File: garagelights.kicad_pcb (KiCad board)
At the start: 4 copper layers, 63.5 x 63.5 mm, 32 parts, among them J1 Conn_01x04, J2 Conn_01x06, Q1 ZVN4206AV, Q2 ZVN4206AV, Q3 ZVN4206AV, U1 NE555P, U2 NE555P, U3 4013, U4 LM7805_TO220, U5 4013

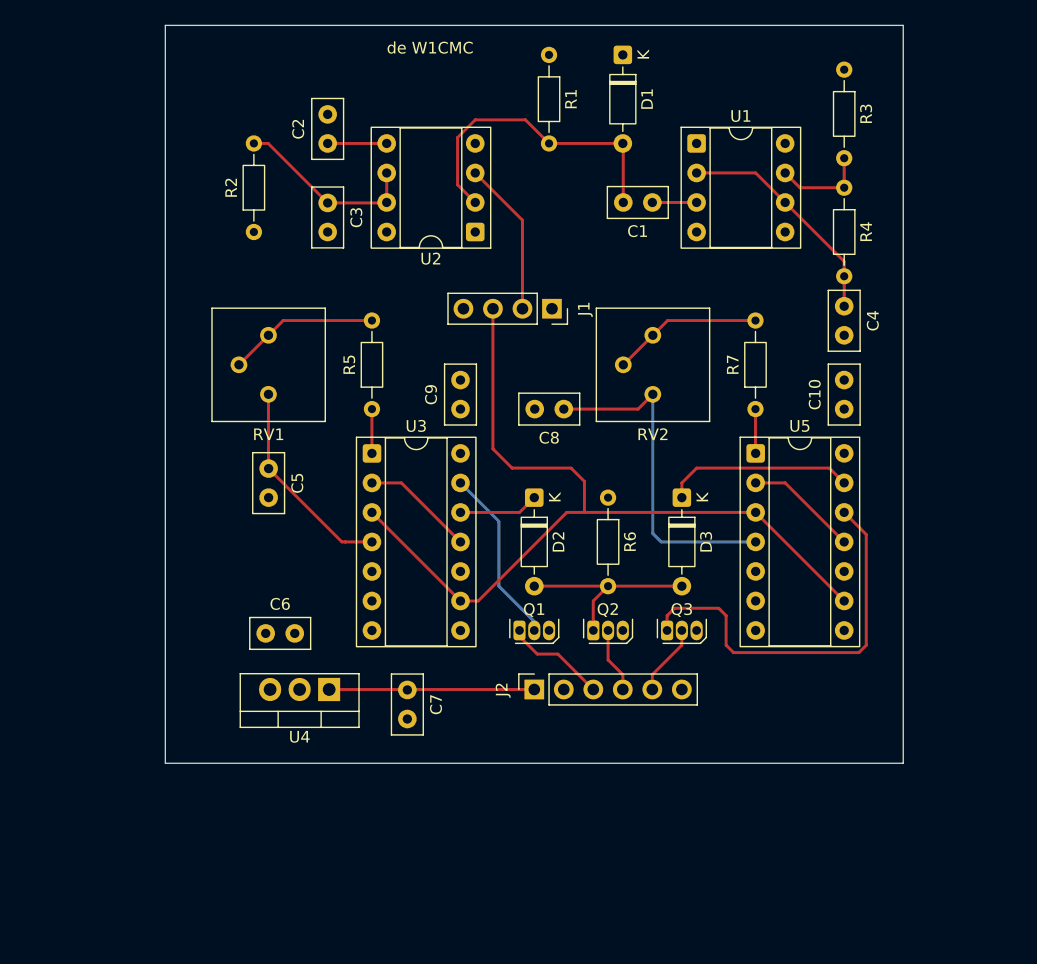
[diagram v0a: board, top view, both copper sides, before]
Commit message: Added screw terminals and mounting holes
Also working towards reducing the number of layers to two.
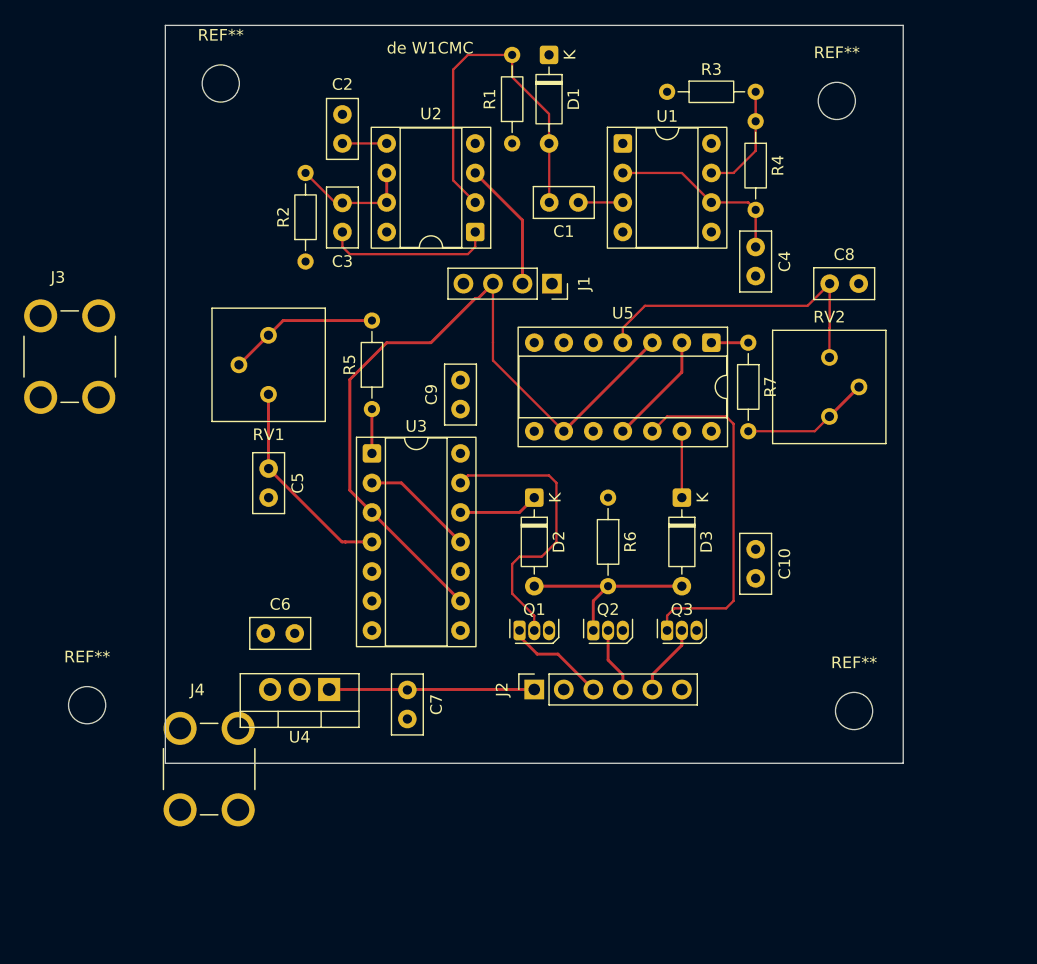
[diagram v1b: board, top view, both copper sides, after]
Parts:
- added J3: Screw_Terminal_01x01, Library:KEYSTONE_8191, F.Cu at (117.5, 92.0)
- added J4: Screw_Terminal_01x01, Library:KEYSTONE_8191, F.Cu at (129.5, 127.5)
- added REF**: MountingHole_3.2mm_M3, MountingHole:MountingHole_3.2mm_M3, F.Cu at (183.5, 70.0)
- added REF**: MountingHole_3.2mm_M3, MountingHole:MountingHole_3.2mm_M3, F.Cu at (185.0, 122.5)
- added REF**: MountingHole_3.2mm_M3, MountingHole:MountingHole_3.2mm_M3, F.Cu at (119.0, 122.0)
- added REF**: MountingHole_3.2mm_M3, MountingHole:MountingHole_3.2mm_M3, F.Cu at (130.5, 68.5)
- C5: value 0.1 -> 1 uF
- moved C8 25.3 mm to (182.9, 85.7), turned to 0 degrees
- moved RV2 16.7 mm to (182.9, 97.2), turned to 0 degrees
- moved R3 15.4 mm to (168.9, 69.2), turned to 0 degrees
- moved C10 14.3 mm to (176.5, 108.6), turned to -90 degrees
- moved U5 10.3 mm to (172.7, 90.8), turned to -90 degrees
- moved R4 9.53 mm to (176.5, 71.8)
- moved C4 9.17 mm to (176.5, 82.6)
- moved R1 8.25 mm to (155.6, 73.7), turned to 90 degrees
- moved C1 6.37 mm to (161.3, 78.7)
- moved D1 6.35 mm to (158.8, 66.0)
- moved U1 6.35 mm to (165.1, 73.7)
- moved R7 5.75 mm to (175.9, 90.8), turned to -90 degrees
- moved R2 5.12 mm to (137.8, 83.8)
- moved J1 2.16 mm to (159.0, 85.7)
- moved C2 1.27 mm to (141.0, 73.7)
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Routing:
- net GND: track 0.00 -> 14.5 mm
- net Net-(D3-K): track 16.3 -> 5.72 mm
- net Net-(Q1-G): track 15.3 -> 25.0 mm
- net Net-(J1-Pin_3): track 73.9 -> 64.7 mm
- net Net-(U2-DIS): track 16.1 -> 10.9 mm
- net Net-(D1-A): track 27.0 -> 31.8 mm
- net Net-(U1-THR): track 19.7 -> 15.9 mm
- net Net-(Q3-G): track 34.2 -> 30.5 mm
- net Net-(U5A-R): track 29.3 -> 27.0 mm
- net Net-(J1-Pin_2): track 13.4 -> 11.2 mm
- net Net-(R7-Pad2): track 13.0 -> 11.1 mm
- net Net-(U1-DIS): track 8.15 -> 9.68 mm
- net Net-(U2-CV): track 5.08 -> 3.81 mm
- net Net-(U5A-Q): track 3.84 -> 3.22 mm

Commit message: Kinda sorta Rev_A
Finished the layout and brought it down to two layers, one of which
is a ground plane. Imported missing 3D models.
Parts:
- removed the REF** at (183.5, 70.0)
- removed the REF** at (185.0, 122.5)
- removed the REF** at (119.0, 122.0)
- removed the REF** at (130.5, 68.5)
- added C11: 0.1, Capacitor_THT:C_Disc_D5.0mm_W2.5mm_P2.50mm, F.Cu at (158.8, 73.0)
- added C12: 0.1, Capacitor_THT:C_Disc_D5.0mm_W2.5mm_P2.50mm, F.Cu at (175.9, 73.3)
- added REF**: MountingHole_3.2mm_M3, MountingHole:MountingHole_3.2mm_M3, F.Cu at (135.3, 135.9)
- added REF**: MountingHole_3.2mm_M3, MountingHole:MountingHole_3.2mm_M3, F.Cu at (192.4, 72.4)
- added REF**: MountingHole_3.2mm_M3, MountingHole:MountingHole_3.2mm_M3, F.Cu at (135.3, 72.4)
- added REF**: MountingHole_3.2mm_M3, MountingHole:MountingHole_3.2mm_M3, F.Cu at (192.4, 135.9)
- moved J3 51.8 mm to (151.1, 131.4)
- moved J4 47.2 mm to (176.5, 131.4)
- moved R7 21.3 mm to (182.2, 111.1), turned to 0 degrees
- moved U5 19.6 mm to (182.2, 108.0), turned to 180 degrees
- moved C8 14.8 mm to (185.4, 100.3), turned to -90 degrees
- moved RV2 12.6 mm to (192.4, 105.4)
- moved D1 12.0 mm to (165.1, 76.2), turned to 90 degrees
- moved RV1 10.8 mm to (135.3, 101.0)
- moved C5 8.81 mm to (142.2, 106.1)
- moved R2 8.64 mm to (144.8, 88.9)
- moved C2 7.43 mm to (148.0, 76.2)
- moved C3 7.43 mm to (148.0, 81.3)
- moved R1 6.84 mm to (161.9, 76.2)
- moved U2 6.84 mm to (158.8, 83.8)
- moved J1 5.45 mm to (163.8, 88.3)
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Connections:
- Q2 pad 1: Net-(D2-A) -> Net-(J2-Pin_4)
- Q2 pad 2: Net-(J2-Pin_4) -> Net-(D2-A)
- Q3 pad 1: Net-(Q3-G) -> Net-(J2-Pin_5)
- Q3 pad 2: Net-(J2-Pin_5) -> Net-(Q3-G)
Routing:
- net Net-(J1-Pin_3): track 64.7 -> 91.3 mm
- net +12V: track 17.7 -> 0.00 mm
- net Net-(U5A-R): track 27.0 -> 10.2 mm
- net GND: track 14.5 -> 0.00 mm
- net Net-(Q3-G): track 30.5 -> 22.1 mm
- net Net-(U3A-R): track 17.9 -> 10.2 mm
- net Net-(J2-Pin_4): track 5.61 -> 9.75 mm
- net Net-(Q1-G): track 25.0 -> 21.8 mm
- net Net-(J2-Pin_3): track 8.75 -> 11.9 mm
- net Net-(D2-A): track 17.0 -> 14.0 mm
- net Net-(R5-Pad2): track 13.0 -> 10.4 mm
- net Net-(U2-DIS): track 10.9 -> 9.29 mm
- net Net-(U1-DIS): track 9.68 -> 11.1 mm
- net Net-(J2-Pin_5): track 6.13 -> 7.58 mm
- net Net-(D2-K): track 6.88 -> 5.72 mm
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- added copper zone on F.Cu, net +12V
- added copper zone on F.Cu, net +5V
- added copper zone on B.Cu, net GND
- removed copper zone on In2.Cu, net +5V
- removed copper zone on In1.Cu, net GND
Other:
- board size 63.5 x 63.5 mm -> 69.8 x 76.2 mm
- copper layers 4 -> 2
- board text added: "Garage Lights Rev A"
